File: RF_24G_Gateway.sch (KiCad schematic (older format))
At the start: 15 parts, among them J1 BME280, J2 LED, J3 MQ135, J4 Mains, J5 Temp, U1 LT8920_Mini, U2 WeMos_mini, U3 MAX485

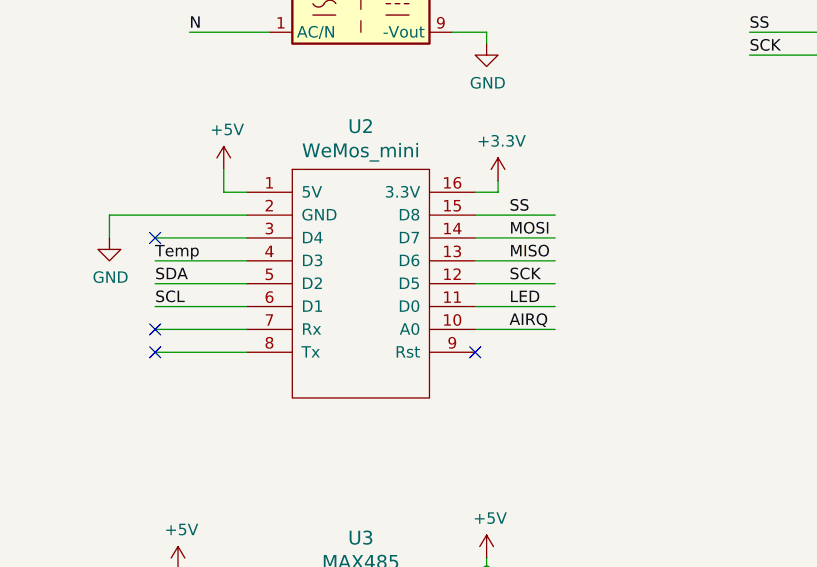
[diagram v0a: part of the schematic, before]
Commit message: Update RF_24G_Gateway.sch
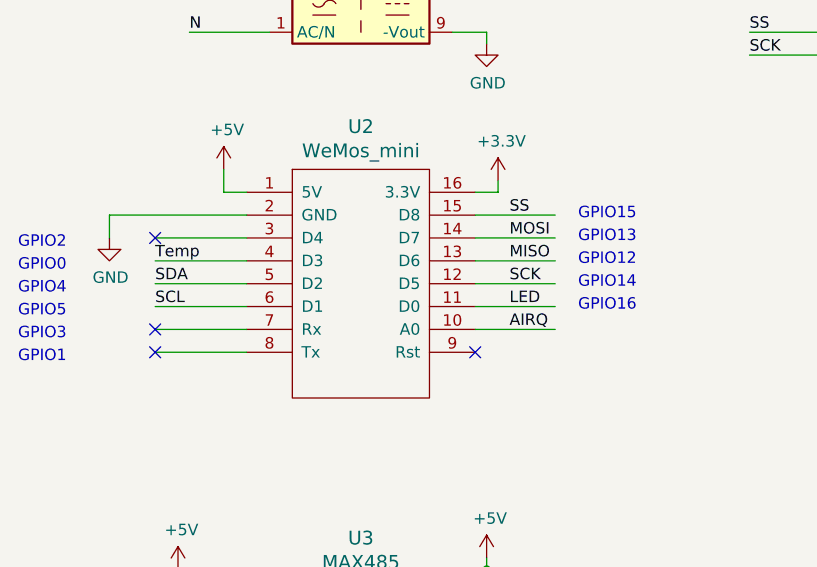
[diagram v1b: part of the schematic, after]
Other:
- note added: "GPIO0"
- note added: "GPIO1"
- note added: "GPIO12"
- note added: "GPIO13"
- note added: "GPIO14"
- note added: "GPIO15"
- note added: "GPIO16"
- note added: "GPIO2"
- note added: "GPIO3"
- note added: "GPIO4"
- note added: "GPIO5"
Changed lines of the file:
@@
 Text Label 3650 3400 0    50   ~ 0
 Temp
+Text Notes 3050 3850 0    50   ~ 0
+GPIO1
+Text Notes 3050 3750 0    50   ~ 0
+GPIO3
+Text Notes 3050 3650 0    50   ~ 0
+GPIO5
+Text Notes 3050 3550 0    50   ~ 0
+GPIO4
+Text Notes 3050 3450 0    50   ~ 0
+GPIO0
+Text Notes 3050 3350 0    50   ~ 0
+GPIO2
+Text Notes 5500 3625 0    50   ~ 0
+GPIO16
+Text Notes 5500 3525 0    50   ~ 0
+GPIO14
+Text Notes 5500 3425 0    50   ~ 0
+GPIO12
+Text Notes 5500 3325 0    50   ~ 0
+GPIO13
+Text Notes 5500 3225 0    50   ~ 0
+GPIO15
 $EndSCHEMATC
